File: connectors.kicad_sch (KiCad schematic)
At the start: 6 parts, among them X501 BH-00105, X502 S4B-PH-SM4-K-TB(LF)(SN)

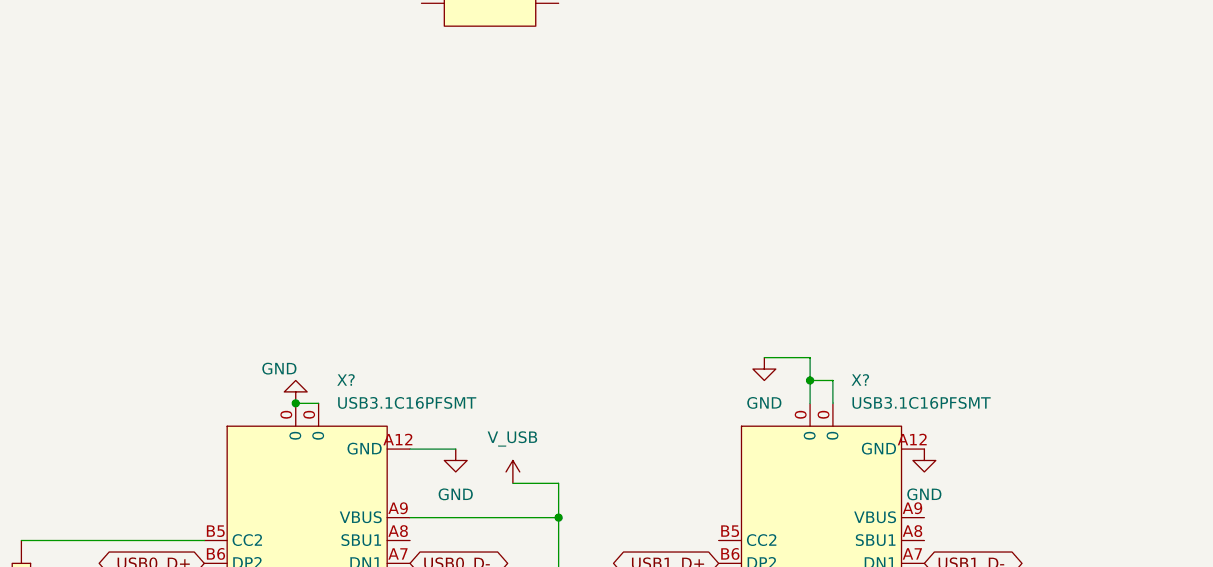
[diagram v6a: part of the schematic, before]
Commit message: add USB ESD Protection
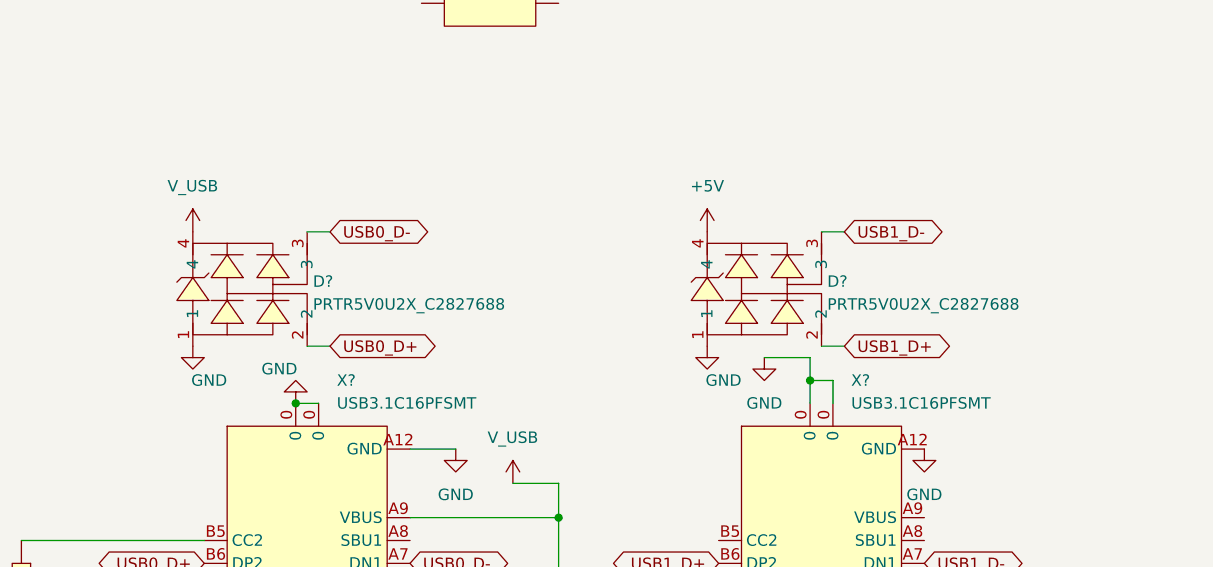
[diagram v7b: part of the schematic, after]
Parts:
- added D? (x2): PRTR5V0U2X_C2827688, SOT-143-4_L2.9-W1.3-P1.92-LS2.4-BL, symbol eduboardv2:PRTR5V0U2X_C2827688
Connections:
- net USB0_D+: now also D?.2
- net USB0_D-: now also D?.3
- net USB1_D+: now also D?.2
- net USB1_D-: now also D?.3
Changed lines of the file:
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@@
+    (stroke (width 0) (type default) (color 0 0 0 0))
+  )
+  (wire (pts (xy 106.68 146.05) (xy 109.22 146.05))
+    (stroke (width 0) (type default) (color 0 0 0 0))
+  )
+  (wire (pts (xy 49.53 133.35) (xy 52.07 133.35))
     (stroke (width 0) (type default) (color 0 0 0 0))
   )
@@
     (stroke (width 0) (type default) (color 0 0 0 0))
   )
+  (wire (pts (xy 49.53 146.05) (xy 52.07 146.05))
+    (stroke (width 0) (type default) (color 0 0 0 0))
+  )
   (wire (pts (xy 105.41 149.86) (xy 105.41 147.32))
     (stroke (width 0) (type default) (color 0 0 0 0))
@@
   )
   (wire (pts (xy 17.78 177.8) (xy 17.78 187.96))
+    (stroke (width 0) (type default) (color 0 0 0 0))
+  )
+  (wire (pts (xy 106.68 133.35) (xy 109.22 133.35))
     (stroke (width 0) (type default) (color 0 0 0 0))
   )
@@
     (at 13.97 30.48 0)
     (effects (font (size 1.27 1.27)) (justify left bottom))
+  )
+  (global_label "USB1_D-" (shape bidirectional) (at 109.22 133.35 0) (fields_autoplaced)
+    (effects (font (size 1.27 1.27)) (justify left))
+    (property "Intersheet References" "${INTERSHEET_REFS}" (id 0) (at 120.4626 133.4294 0)
+      (effects (font (size 1.27 1.27)) (justify left) hide)
+    )
   )
   (global_label "USB1_D+" (shape bidirectional) (at 95.25 170.18 180) (fields_autoplaced)
@@
     )
   )
+  (global_label "USB0_D-" (shape bidirectional) (at 52.07 133.35 0) (fields_autoplaced)
+    (effects (font (size 1.27 1.27)) (justify left))
+    (property "Intersheet References" "${INTERSHEET_REFS}" (id 0) (at 63.3126 133.4294 0)
+      (effects (font (size 1.27 1.27)) (justify left) hide)
+    )
+  )
   (global_label "USB1_D-" (shape bidirectional) (at 118.11 170.18 0) (fields_autoplaced)
     (effects (font (size 1.27 1.27)) (justify left))
@@
     )
   )
+  (global_label "USB1_D+" (shape bidirectional) (at 109.22 146.05 0) (fields_autoplaced)
+    (effects (font (size 1.27 1.27)) (justify left))
+    (property "Intersheet References" "${INTERSHEET_REFS}" (id 0) (at 120.4626 146.1294 0)
+      (effects (font (size 1.27 1.27)) (justify left) hide)
+    )
+  )
   (global_label "USB0_D+" (shape bidirectional) (at 60.96 172.72 0) (fields_autoplaced)
     (effects (font (size 1.27 1.27)) (justify left))
@@
     )
   )
+  (global_label "USB0_D+" (shape bidirectional) (at 52.07 146.05 0) (fields_autoplaced)
+    (effects (font (size 1.27 1.27)) (justify left))
+    (property "Intersheet References" "${INTERSHEET_REFS}" (id 0) (at 63.3126 146.1294 0)
+      (effects (font (size 1.27 1.27)) (justify left) hide)
+    )
+  )
   (symbol (lib_name "GND_16") (lib_id "eduboardv2:GND") (at 66.04 157.48 0) (unit 1)
     (in_bom yes) (on_board yes) (fields_autoplaced)
@@
     (pin "1")
   )
+  (symbol (lib_name "+5V_1") (lib_id "eduboardv2:+5V") (at 93.98 133.35 0) (unit 1)
+    (in_bom yes) (on_board yes) (fields_autoplaced)
+    (property "Reference" "#PWR?" (id 0) (at 93.98 137.16 0)
+      (effects (font (size 1.27 1.27)) hide)
+    )
+    (property "Value" "+5V" (id 1) (at 93.98 128.27 0))
+    (property "Footprint" "" (id 2) (at 93.98 133.35 0)
+      (effects (font (size 1.27 1.27)) hide)
+    )
+    (property "Datasheet" "" (id 3) (at 93.98 133.35 0)
+      (effects (font (size 1.27 1.27)) hide)
+    )
+    (pin "1")
+  )
+  (symbol (lib_name "GND_17") (lib_id "eduboardv2:GND") (at 93.98 146.05 0) (unit 1)
+    (in_bom yes) (on_board yes)
+    (property "Reference" "#PWR?" (id 0) (at 93.98 152.4 0)
+      (effects (font (size 1.27 1.27)) hide)
+    )
+    (property "Value" "GND" (id 1) (at 97.79 149.86 0)
+      (effects (font (size 1.27 1.27)) (justify right))
+    )
+    (property "Footprint" "" (id 2) (at 93.98 146.05 0)
+      (effects (font (size 1.27 1.27)) hide)
+    )
+    (property "Datasheet" "" (id 3) (at 93.98 146.05 0)
+      (effects (font (size 1.27 1.27)) hide)
+    )
+    (pin "1")
+  )
   (symbol (lib_name "0402WGF5101TCE_1") (lib_id "eduboardv2:0402WGF5101TCE") (at 17.78 172.72 270) (unit 1)
     (in_bom yes) (on_board yes) (fields_autoplaced)
@@
     (pin "1")
     (pin "2")
+  )
+  (symbol (lib_id "eduboardv2:PRTR5V0U2X_C2827688") (at 41.91 140.97 0) (unit 1)
+    (in_bom yes) (on_board yes) (fields_autoplaced)
+    (property "Reference" "D?" (id 0) (at 50.165 138.8653 0)
+      (effects (font (size 1.27 1.27)) (justify left))
+    )
+    (property "Value" "PRTR5V0U2X_C2827688" (id 1) (at 50.165 141.4022 0)
+      (effects (font (size 1.27 1.27)) (justify left))
+    )
+    (property "Footprint" "SOT-143-4_L2.9-W1.3-P1.92-LS2.4-BL" (id 2) (at 41.91 153.67 0)
+      (effects (font (size 1.27 1.27)) hide)
+    )
+    (property "Datasheet" "" (id 3) (at 41.91 140.97 0)
+      (effects (font (size 1.27 1.27)) hide)
+    )
+    (property "Manufacturer" "TECH PUBLIC(台舟)" (id 4) (at 41.91 156.21 0)
+      (effects (font (size 1.27 1.27)) hide)
+    )
+    (property "LCSC Part" "C2827688" (id 5) (at 41.91 158.75 0)
+      (effects (font (size 1.27 1.27)) hide)
+    )
+    (property "JLC Part" "Extended Part" (id 6) (at 41.91 161.29 0)
+      (effects (font (size 1.27 1.27)) hide)
+    )
+    (pin "1")
+    (pin "2")
+    (pin "3")
+    (pin "4")
   )
   (symbol (lib_name "GND_11") (lib_id "eduboardv2:GND") (at 48.26 190.5 0) (unit 1)
@@
     )
     (pin "1")
+  )
+  (symbol (lib_id "eduboardv2:PRTR5V0U2X_C2827688") (at 99.06 140.97 0) (unit 1)
+    (in_bom yes) (on_board yes) (fields_autoplaced)
+    (property "Reference" "D?" (id 0) (at 107.315 138.8653 0)
+      (effects (font (size 1.27 1.27)) (justify left))
+    )
+    (property "Value" "PRTR5V0U2X_C2827688" (id 1) (at 107.315 141.4022 0)
+      (effects (font (size 1.27 1.27)) (justify left))
+    )
+    (property "Footprint" "SOT-143-4_L2.9-W1.3-P1.92-LS2.4-BL" (id 2) (at 99.06 153.67 0)
+      (effects (font (size 1.27 1.27)) hide)
+    )
+    (property "Datasheet" "" (id 3) (at 99.06 140.97 0)
+      (effects (font (size 1.27 1.27)) hide)
+    )
+    (property "Manufacturer" "TECH PUBLIC(台舟)" (id 4) (at 99.06 156.21 0)
+      (effects (font (size 1.27 1.27)) hide)
+    )
+    (property "LCSC Part" "C2827688" (id 5) (at 99.06 158.75 0)
+      (effects (font (size 1.27 1.27)) hide)
+    )
+    (property "JLC Part" "Extended Part" (id 6) (at 99.06 161.29 0)
+      (effects (font (size 1.27 1.27)) hide)
+    )
+    (pin "1")
+    (pin "2")
+    (pin "3")
+    (pin "4")
   )
   (symbol (lib_id "eduboardv2:USB3.1C16PFSMT") (at 106.68 171.45 0) (unit 1)
@@
     (pin "B8")
   )
+  (symbol (lib_name "GND_17") (lib_id "eduboardv2:GND") (at 36.83 146.05 0) (unit 1)
+    (in_bom yes) (on_board yes)
+    (property "Reference" "#PWR?" (id 0) (at 36.83 152.4 0)
+      (effects (font (size 1.27 1.27)) hide)
+    )
+    (property "Value" "GND" (id 1) (at 40.64 149.86 0)
+      (effects (font (size 1.27 1.27)) (justify right))
+    )
+    (property "Footprint" "" (id 2) (at 36.83 146.05 0)
+      (effects (font (size 1.27 1.27)) hide)
+    )
+    (property "Datasheet" "" (id 3) (at 36.83 146.05 0)
+      (effects (font (size 1.27 1.27)) hide)
+    )
+    (pin "1")
+  )
   (symbol (lib_name "GND_12") (lib_id "eduboardv2:GND") (at 17.78 187.96 0) (unit 1)
     (in_bom yes) (on_board yes) (fields_autoplaced)
@@
     (pin "B8")
   )
+  (symbol (lib_id "eduboardv2:V_USB") (at 36.83 133.35 0) (unit 1)
+    (in_bom yes) (on_board yes) (fields_autoplaced)
+    (property "Reference" "#PWR?" (id 0) (at 36.83 137.16 0)
+      (effects (font (size 1.27 1.27)) hide)
+    )
+    (property "Value" "V_USB" (id 1) (at 36.83 128.27 0))
+    (property "Footprint" "" (id 2) (at 36.83 133.35 0)
+      (effects (font (size 1.27 1.27)) hide)
+    )
+    (property "Datasheet" "" (id 3) (at 36.83 133.35 0)
+      (effects (font (size 1.27 1.27)) hide)
+    )
+    (pin "1")
+  )
   (symbol (lib_id "eduboardv2:BH-00105") (at 69.85 80.01 0) (unit 1)

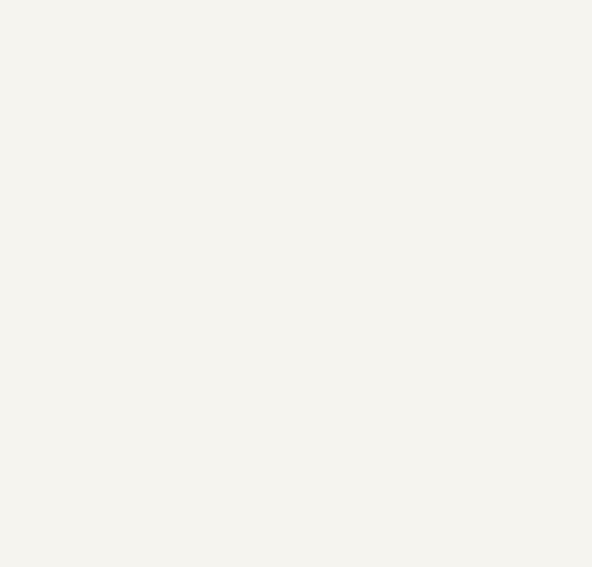
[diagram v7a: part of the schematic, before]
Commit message: add WS2812 Output Connector and add Level shifter to WS2812 input for 3.3V->5V conversion
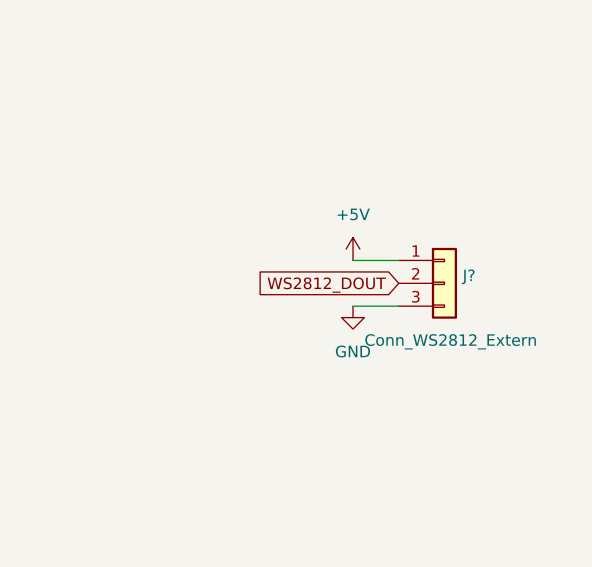
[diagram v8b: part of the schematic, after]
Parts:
- added J?: Conn_WS2812_Extern, symbol Connector_Generic:Conn_01x03
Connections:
- new net WS2812_DOUT: J?.2 (Pin_2)
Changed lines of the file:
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@@
+    (stroke (width 0) (type default) (color 0 0 0 0))
+  )
+  (wire (pts (xy 261.62 153.67) (xy 266.7 153.67))
+    (stroke (width 0) (type default) (color 0 0 0 0))
+  )
+  (wire (pts (xy 261.62 158.75) (xy 266.7 158.75))
     (stroke (width 0) (type default) (color 0 0 0 0))
   )
@@
     )
   )
+  (global_label "WS2812_DOUT" (shape input) (at 266.7 156.21 180) (fields_autoplaced)
+    (effects (font (size 1.27 1.27)) (justify right))
+    (property "Intersheet References" "${INTERSHEET_REFS}" (id 0) (at 250.9217 156.1306 0)
+      (effects (font (size 1.27 1.27)) (justify right) hide)
+    )
+  )
   (global_label "USB0_D+" (shape bidirectional) (at 52.07 146.05 0) (fields_autoplaced)
     (effects (font (size 1.27 1.27)) (justify left))
@@
     (pin "1")
   )
+  (symbol (lib_name "+5V_1") (lib_id "eduboardv2:+5V") (at 261.62 153.67 0) (unit 1)
+    (in_bom yes) (on_board yes) (fields_autoplaced)
+    (property "Reference" "#PWR?" (id 0) (at 261.62 157.48 0)
+      (effects (font (size 1.27 1.27)) hide)
+    )
+    (property "Value" "+5V" (id 1) (at 261.62 148.59 0))
+    (property "Footprint" "" (id 2) (at 261.62 153.67 0)
+      (effects (font (size 1.27 1.27)) hide)
+    )
+    (property "Datasheet" "" (id 3) (at 261.62 153.67 0)
+      (effects (font (size 1.27 1.27)) hide)
+    )
+    (pin "1")
+  )
   (symbol (lib_id "eduboardv2:0402WGF5101TCE") (at 80.01 180.34 90) (unit 1)
     (in_bom yes) (on_board yes) (fields_autoplaced)
@@
     )
     (property "Datasheet" "" (id 3) (at 80.01 189.23 0)
+      (effects (font (size 1.27 1.27)) hide)
+    )
+    (pin "1")
+  )
+  (symbol (lib_name "GND_14") (lib_id "eduboardv2:GND") (at 261.62 158.75 0) (unit 1)
+    (in_bom yes) (on_board yes) (fields_autoplaced)
+    (property "Reference" "#PWR?" (id 0) (at 261.62 165.1 0)
+      (effects (font (size 1.27 1.27)) hide)
+    )
+    (property "Value" "GND" (id 1) (at 261.62 163.83 0))
+    (property "Footprint" "" (id 2) (at 261.62 158.75 0)
+      (effects (font (size 1.27 1.27)) hide)
+    )
+    (property "Datasheet" "" (id 3) (at 261.62 158.75 0)
       (effects (font (size 1.27 1.27)) hide)
     )
@@
     (pin "1")
   )
+  (symbol (lib_id "Connector_Generic:Conn_01x03") (at 271.78 156.21 0) (unit 1)
+    (in_bom yes) (on_board yes)
+    (property "Reference" "J?" (id 0) (at 273.812 155.3753 0)
+      (effects (font (size 1.27 1.27)) (justify left))
+    )
+    (property "Value" "Conn_WS2812_Extern" (id 1) (at 262.89 162.56 0)
+      (effects (font (size 1.27 1.27)) (justify left))
+    )
+    (property "Footprint" "" (id 2) (at 271.78 156.21 0)
+      (effects (font (size 1.27 1.27)) hide)
+    )
+    (property "Datasheet" "~" (id 3) (at 271.78 156.21 0)
+      (effects (font (size 1.27 1.27)) hide)
+    )
+    (pin "1")
+    (pin "2")
+    (pin "3")
+  )
   (symbol (lib_id "eduboardv2:PRTR5V0U2X_C2827688") (at 99.06 140.97 0) (unit 1)
